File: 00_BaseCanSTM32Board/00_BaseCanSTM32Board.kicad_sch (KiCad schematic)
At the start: 42 parts, among them J1 I2C1_5, J2 I2C2_5, J3 CAN1, J4 CAN2, J5 In App Prog, J6 DEBUG, SW1 RESET, SW2 BOOT0, U1 STM32G474RETx, U2 AMS1117-3.3, U3 MCP2558FD-xSN, Y1 16MHz

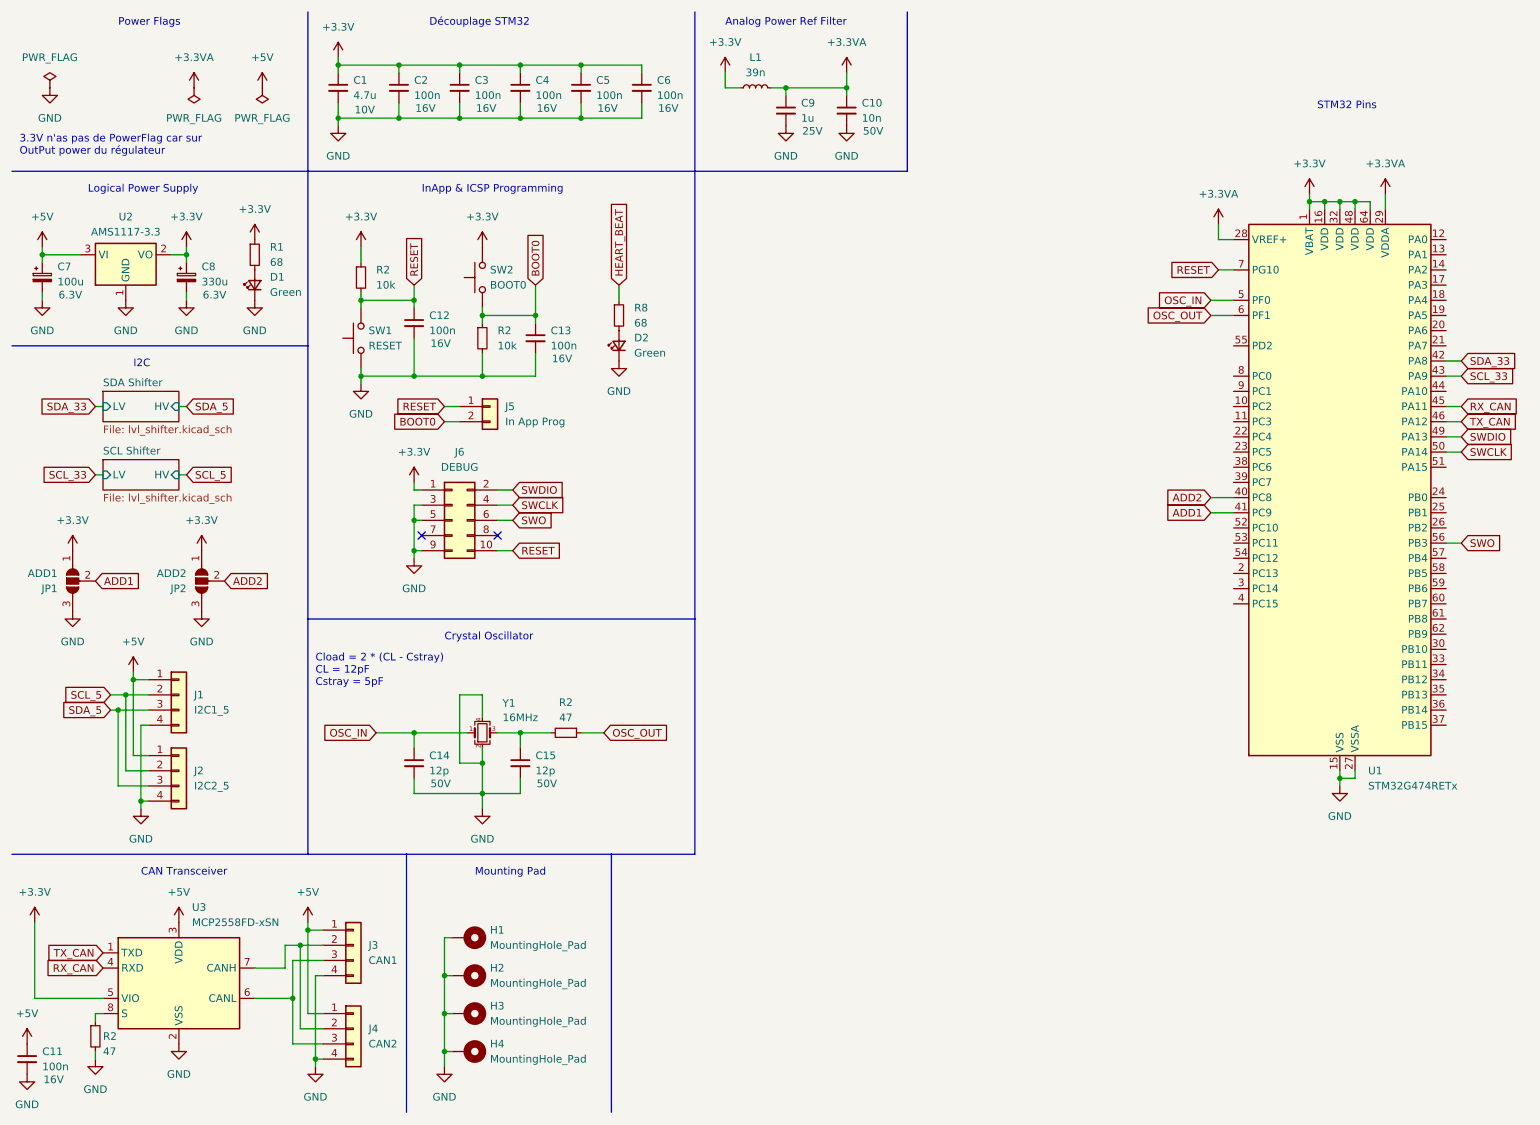
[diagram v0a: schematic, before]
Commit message: Fix base PCB STM32 CAN
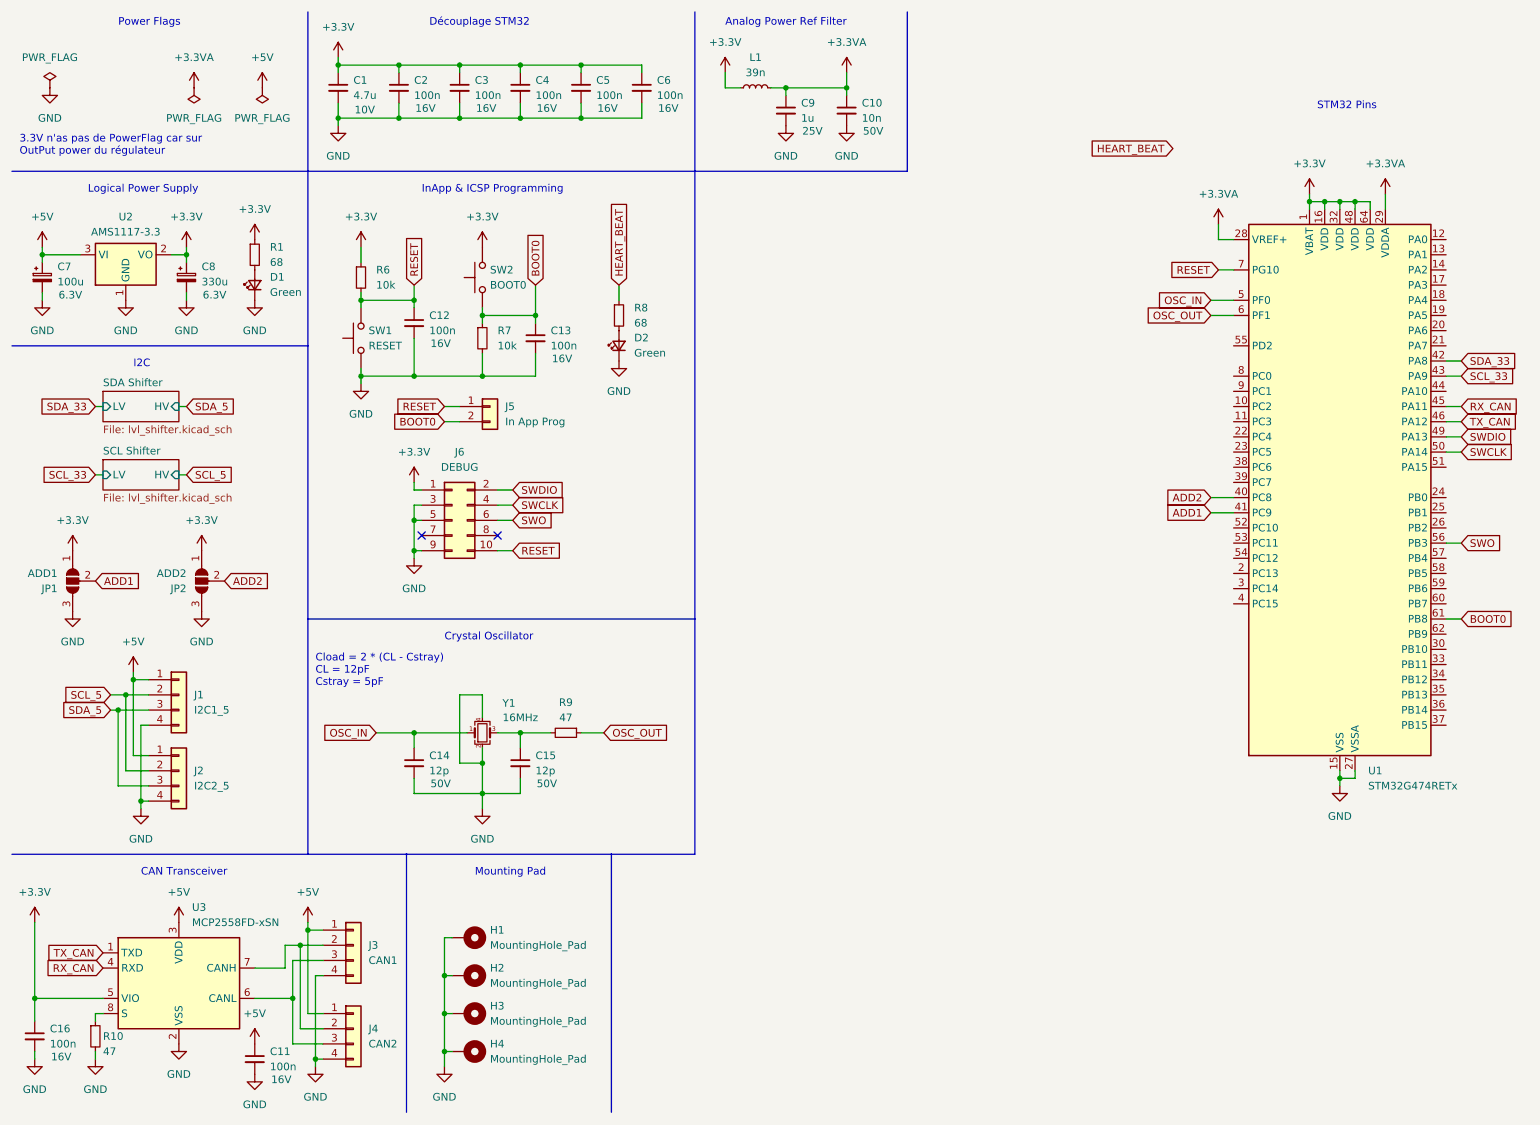
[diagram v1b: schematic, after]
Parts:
- added C16: 100n, Capacitor_SMD:C_0402_1005Metric_Pad0.74x0.62mm_HandSolder, symbol Device:C_Small
- renumbered R2 to R10, R2 to R6, R2 to R7, R2 to R9
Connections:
- net +3.3V: now also C16.1
- net BOOT0: now also U1.61 (PB8)
- net GND: now also C16.2
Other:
- moved on the sheet: C11

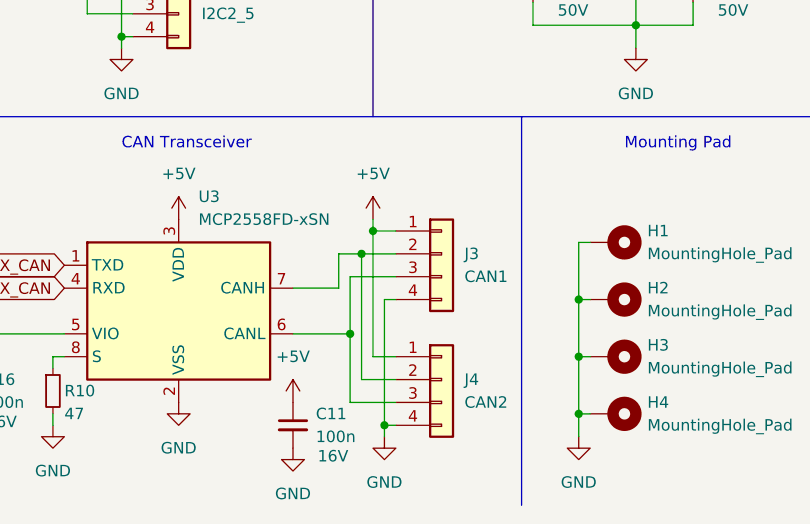
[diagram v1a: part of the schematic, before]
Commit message: Fix CAN connections to improve routing on Base Board
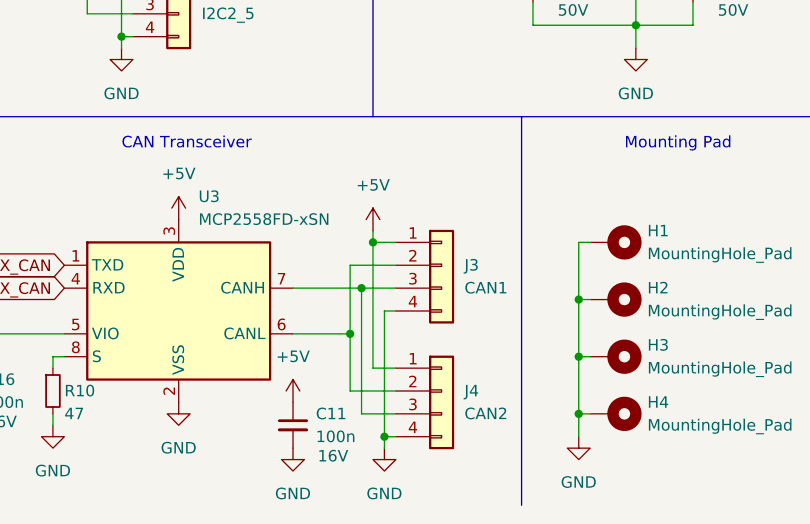
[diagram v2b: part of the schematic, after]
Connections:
- net at J3.3 (Pin_3), J4.3 (Pin_3): now also U3.7 (CANH); no longer U3.6 (CANL)
- net at J3.2 (Pin_2), J4.2 (Pin_2): now also U3.6 (CANL); no longer U3.7 (CANH)
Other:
- moved on the sheet: J3, J4
